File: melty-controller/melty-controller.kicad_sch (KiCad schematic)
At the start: 39 parts, among them J1 Conn_01x02_Male, J2 soicbite, J3 esc_io, Q1 2N7002ET1G, U1 ESP32-PICO-D4, U2 MT2492, U3 MMA1200KEG, U4 HT7250

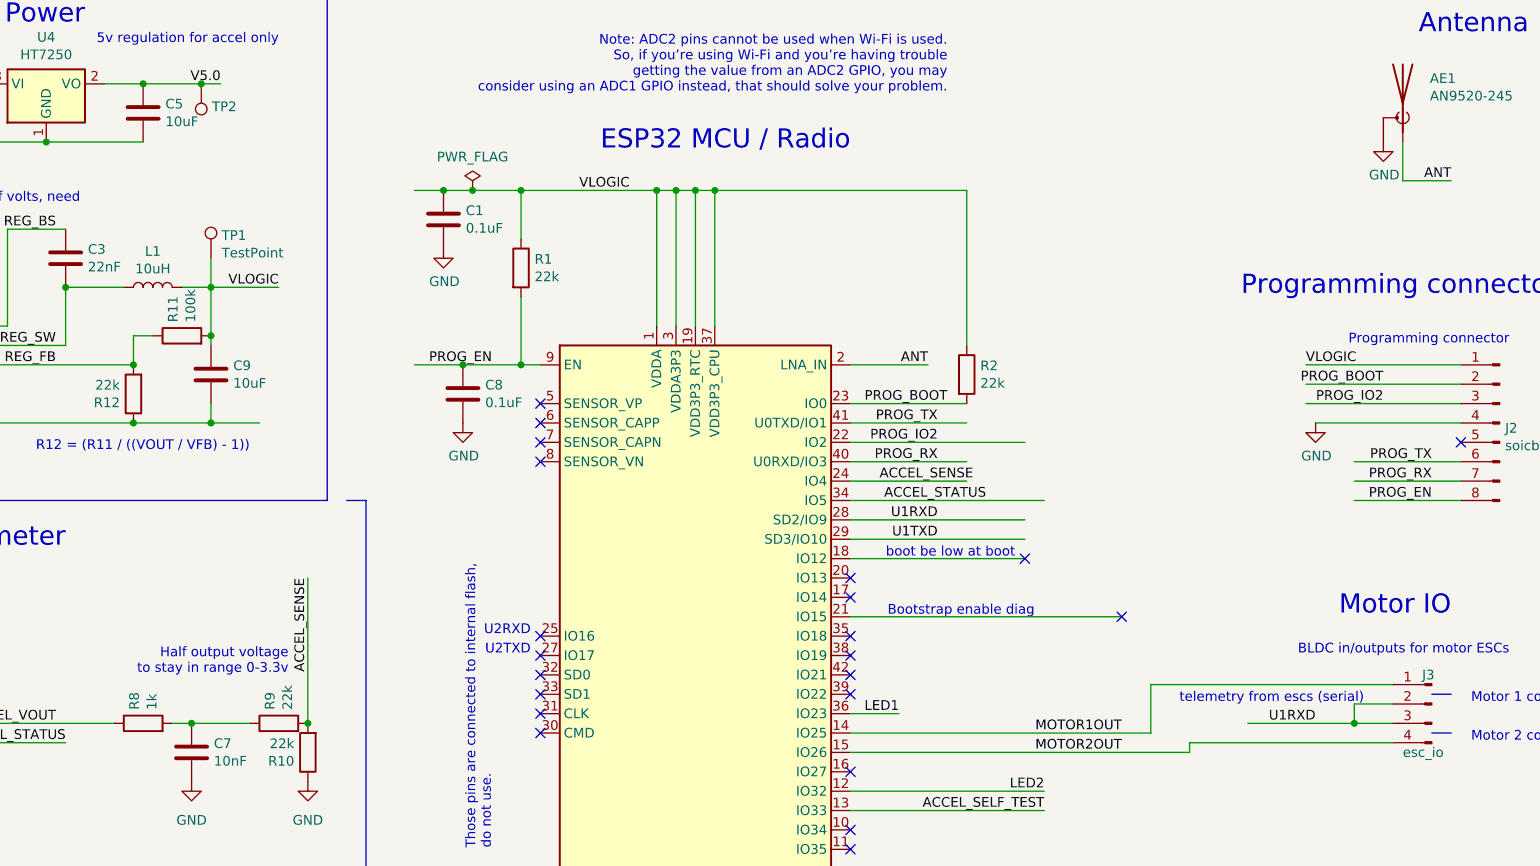
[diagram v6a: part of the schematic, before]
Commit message: Add more testpoints and minor fixes
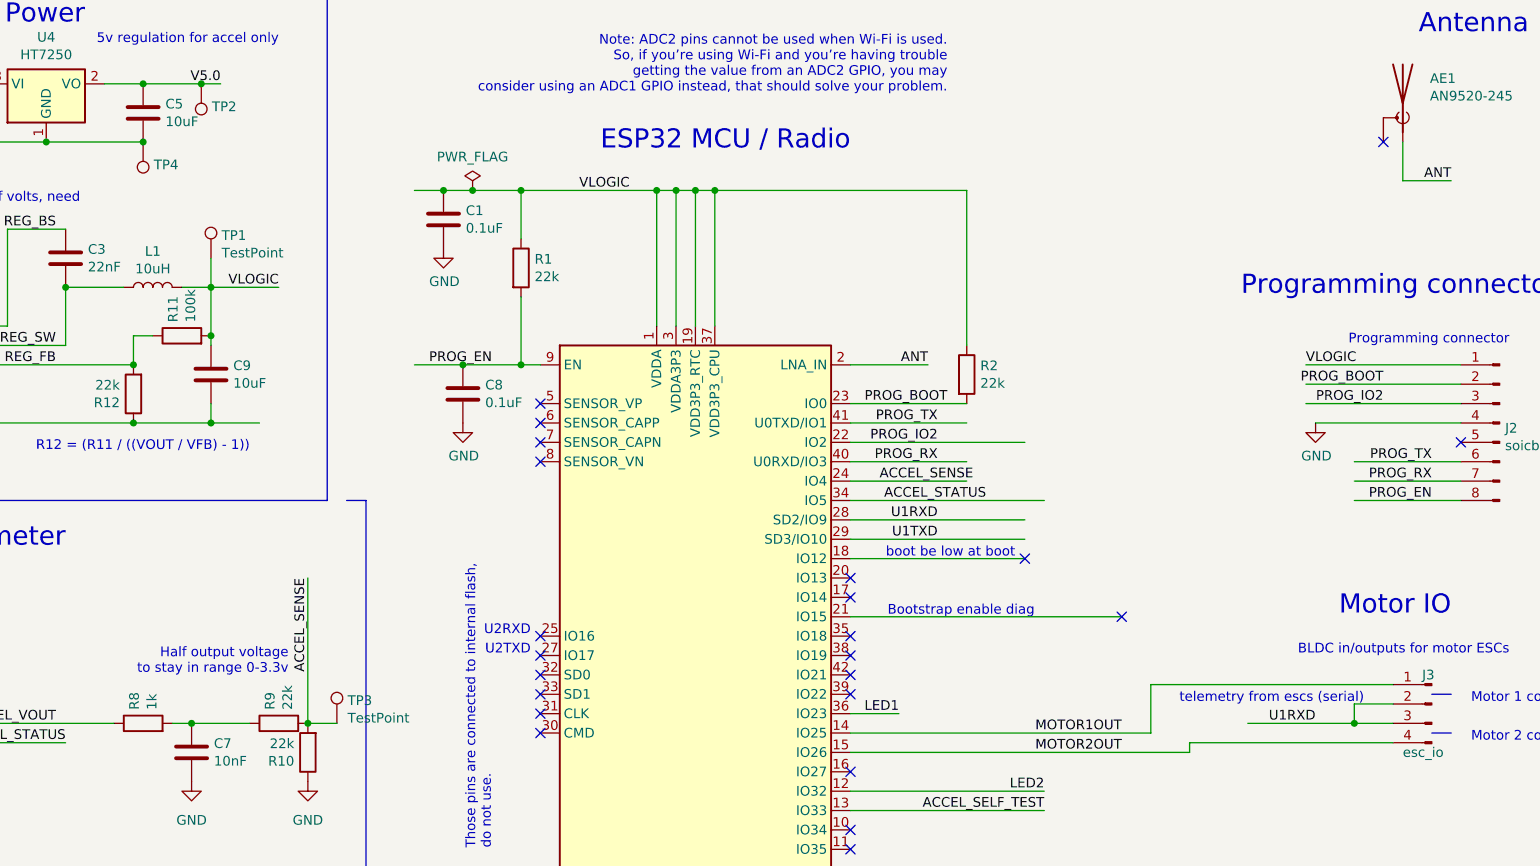
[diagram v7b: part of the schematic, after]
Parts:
- added TP3, TP4: TestPoint, TestPoint:TestPoint_Pad_1.5x1.5mm, symbol Connector:TestPoint
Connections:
- net ACCEL_SENSE: now also TP3.1
- net GND: now also TP4.1; no longer AE1.2 (Shield)
- no-connect marks 22 -> 23
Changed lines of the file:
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@@
   (junction (at 77.47 71.12) (diameter 0) (color 0 0 0 0))
   (junction (at 78.74 26.67) (diameter 0) (color 0 0 0 0))
+  (junction (at 78.74 34.29) (diameter 0) (color 0 0 0 0))
   (junction (at 83.82 173.99) (diameter 0) (color 0 0 0 0))
   (junction (at 85.09 110.49) (diameter 0) (color 0 0 0 0))
@@
   (junction (at 153.67 40.64) (diameter 0) (color 0 0 0 0))
   (junction (at 237.49 110.49) (diameter 0) (color 0 0 0 0))
-  (no_connect (at 171.45 99.06))
-  (no_connect (at 171.45 116.84))
-  (no_connect (at 171.45 101.6))
+  (no_connect (at 130.81 71.12))
+  (no_connect (at 130.81 68.58))
+  (no_connect (at 171.45 104.14))
   (no_connect (at 251.46 73.66))
-  (no_connect (at 130.81 68.58))
+  (no_connect (at 171.45 127))
+  (no_connect (at 207.01 96.52))
+  (no_connect (at 194.31 88.9))
   (no_connect (at 171.45 124.46))
-  (no_connect (at 171.45 91.44))
+  (no_connect (at 171.45 106.68))
+  (no_connect (at 130.81 101.6))
+  (no_connect (at 130.81 111.76))
+  (no_connect (at 171.45 93.98))
   (no_connect (at 130.81 109.22))
-  (no_connect (at 207.01 96.52))
   (no_connect (at 130.81 73.66))
   (no_connect (at 130.81 106.68))
-  (no_connect (at 171.45 127))
+  (no_connect (at 171.45 91.44))
+  (no_connect (at 130.81 104.14))
+  (no_connect (at 171.45 99.06))
   (no_connect (at 130.81 76.2))
-  (no_connect (at 171.45 104.14))
-  (no_connect (at 171.45 93.98))
-  (no_connect (at 130.81 71.12))
-  (no_connect (at 130.81 101.6))
-  (no_connect (at 171.45 106.68))
-  (no_connect (at 130.81 104.14))
-  (no_connect (at 130.81 111.76))
-  (no_connect (at 194.31 88.9))
+  (no_connect (at 171.45 116.84))
   (no_connect (at 130.81 99.06))
+  (no_connect (at 171.45 101.6))
+  (no_connect (at 241.3 34.29))
   (wire (pts (xy 15.24 118.11) (xy 33.02 118.11))
     (stroke (width 0) (type solid) (color 0 0 0 0))
@@
   )
   (wire (pts (xy 100.33 91.44) (xy 100.33 110.49))
+    (stroke (width 0) (type solid) (color 0 0 0 0))
+  )
+  (wire (pts (xy 100.33 110.49) (xy 104.14 110.49))
     (stroke (width 0) (type solid) (color 0 0 0 0))
   )
@@
     )
   )
+  (symbol (lib_id "Connector:TestPoint") (at 78.74 34.29 0) (mirror x) (unit 1)
+    (in_bom yes) (on_board yes)
+    (property "Reference" "TP4" (id 0) (at 80.1371 37.2809 0)
+      (effects (font (size 1.27 1.27)) (justify left))
+    )
+    (property "Value" "TestPoint" (id 1) (at 80.1371 34.9822 0)
+      (effects (font (size 1.27 1.27)) (justify left) hide)
+    )
+    (property "Footprint" "TestPoint:TestPoint_Pad_1.5x1.5mm" (id 2) (at 83.82 34.29 0)
+      (effects (font (size 1.27 1.27)) hide)
+    )
+    (property "Datasheet" "~" (id 3) (at 83.82 34.29 0)
+      (effects (font (size 1.27 1.27)) hide)
+    )
+  )
   (symbol (lib_id "Connector:TestPoint") (at 86.36 26.67 0) (mirror x) (unit 1)
     (in_bom yes) (on_board yes)
@@
     )
     (property "Datasheet" "~" (id 3) (at 92.71 49.53 0)
+      (effects (font (size 1.27 1.27)) hide)
+    )
+  )
+  (symbol (lib_id "Connector:TestPoint") (at 104.14 110.49 0) (unit 1)
+    (in_bom yes) (on_board yes)
+    (property "Reference" "TP3" (id 0) (at 105.5371 107.4991 0)
+      (effects (font (size 1.27 1.27)) (justify left))
+    )
+    (property "Value" "TestPoint" (id 1) (at 105.5371 109.7978 0)
+      (effects (font (size 1.27 1.27)) (justify left))
+    )
+    (property "Footprint" "TestPoint:TestPoint_Pad_1.5x1.5mm" (id 2) (at 109.22 110.49 0)
+      (effects (font (size 1.27 1.27)) hide)
+    )
+    (property "Datasheet" "~" (id 3) (at 109.22 110.49 0)
       (effects (font (size 1.27 1.27)) hide)
     )
@@
     )
     (property "Datasheet" "" (id 3) (at 232.41 71.12 0)
-      (effects (font (size 1.27 1.27)) hide)
-    )
-  )
-  (symbol (lib_id "power:GND") (at 241.3 34.29 0) (unit 1)
-    (in_bom yes) (on_board yes)
-    (property "Reference" "#PWR04" (id 0) (at 241.3 40.64 0)
-      (effects (font (size 1.27 1.27)) hide)
-    )
-    (property "Value" "GND" (id 1) (at 241.4143 38.6144 0))
-    (property "Footprint" "" (id 2) (at 241.3 34.29 0)
-      (effects (font (size 1.27 1.27)) hide)
-    )
-    (property "Datasheet" "" (id 3) (at 241.3 34.29 0)
       (effects (font (size 1.27 1.27)) hide)
     )
@@
       (reference "#PWR03") (unit 1)
     )
-    (path "/443ac6f1-680f-4598-9ffb-e96eef2d7f1a"
-      (reference "#PWR04") (unit 1)
-    )
     (path "/f0666eca-ac18-44f5-a55d-51e5ed066097"
       (reference "#PWR05") (unit 1)
@@
       (reference "TP2") (unit 1)
     )
+    (path "/6a4587a3-cf5e-4524-a8c1-3f68fefec719"
+      (reference "TP3") (unit 1)
+    )
+    (path "/351c7b9e-3c3a-4f95-85df-106866db9b8b"
+      (reference "TP4") (unit 1)
+    )
     (path "/b91b9274-ad09-4c59-9311-b440a305e6c7"

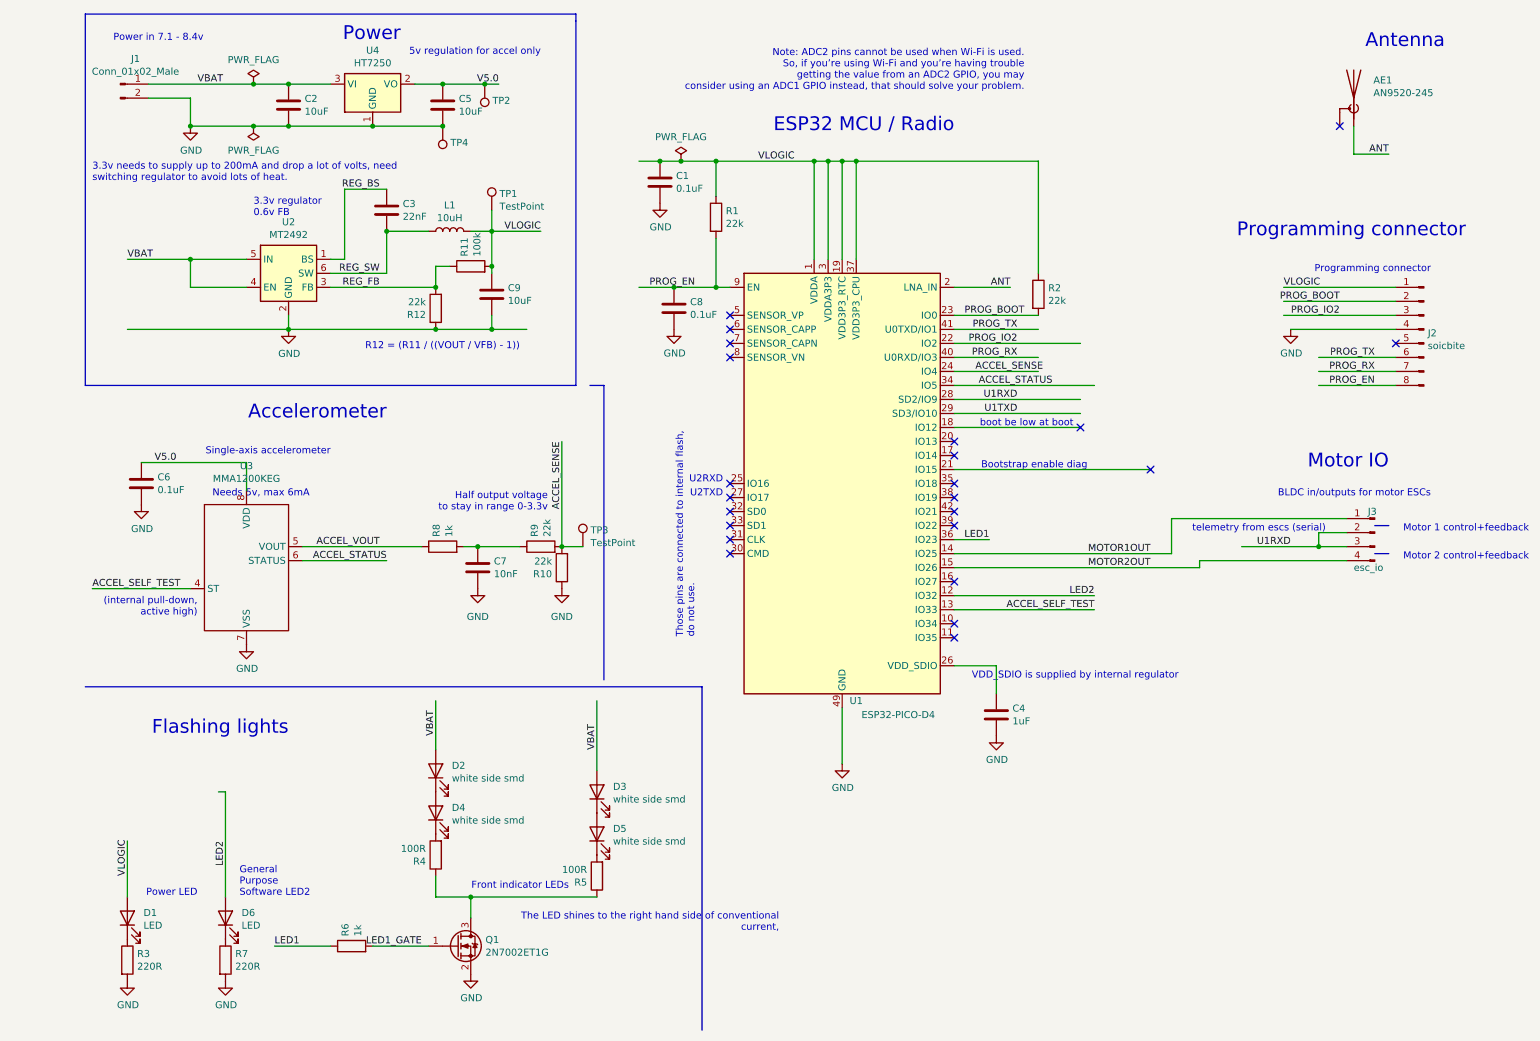
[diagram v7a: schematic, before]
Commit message: correct some doc errors on schematic
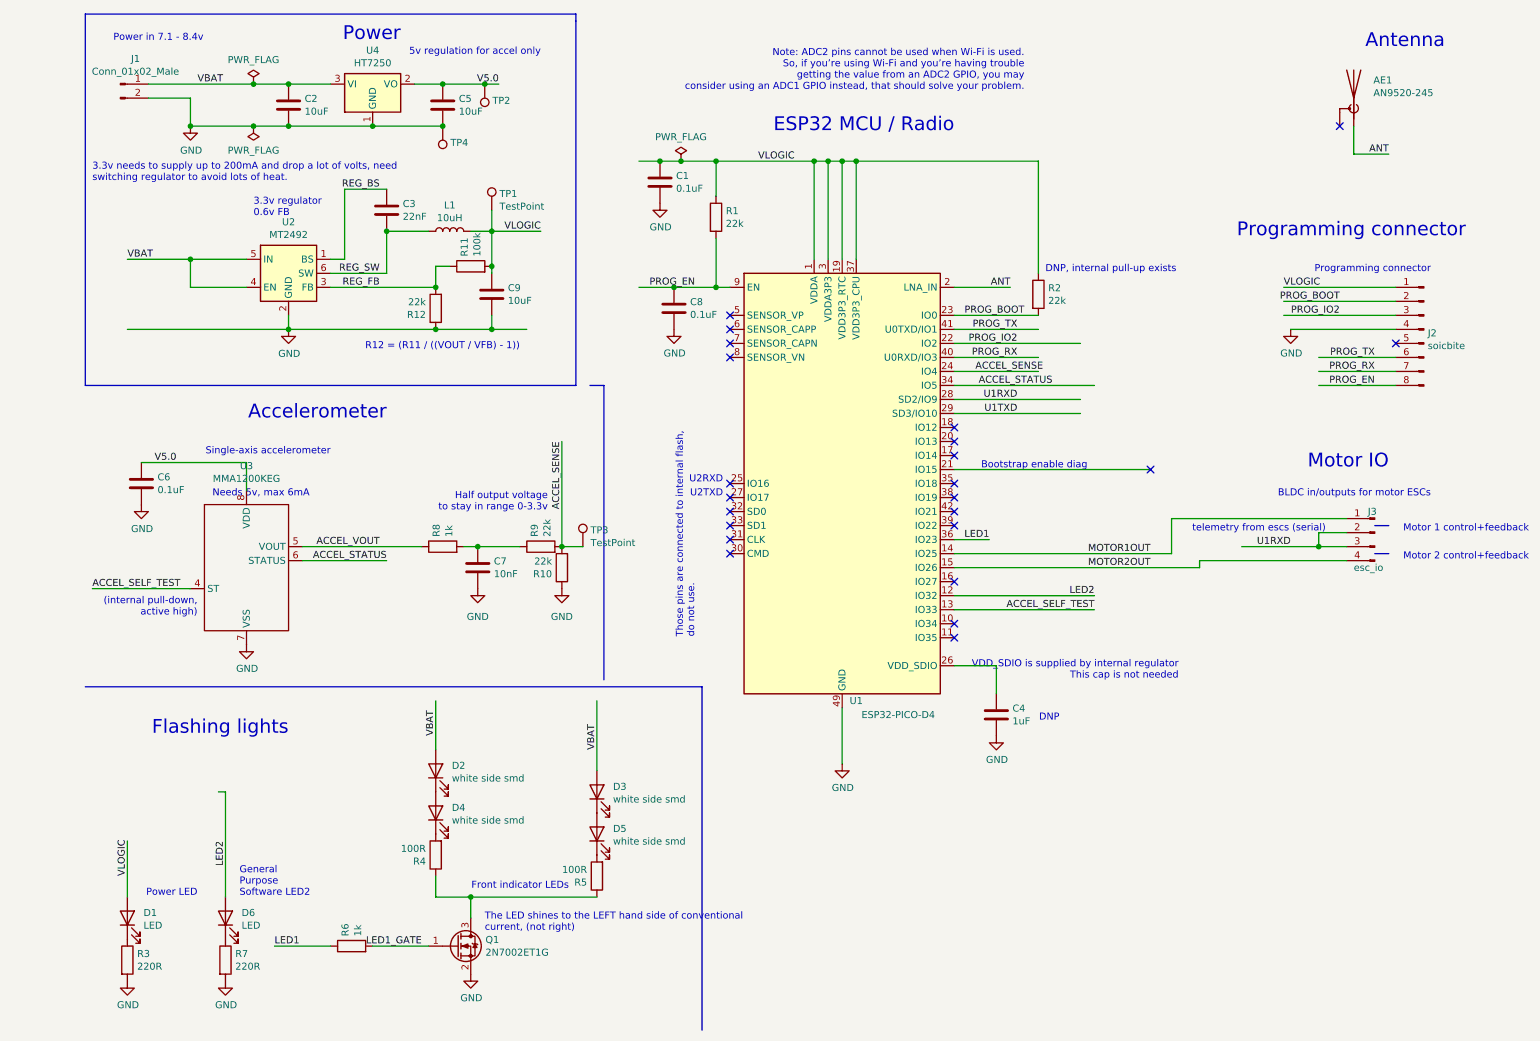
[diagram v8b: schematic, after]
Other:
- note added: "DNP"
- note added: "DNP, internal pull-up exists"
- note added: "The LED shines to the LEFT hand side of conventional current, (not right)"
- note added: "VDD_SDIO is supplied by internal regulator This cap is not needed"
- note removed: "The LED shines to the right hand side of conventional current,"
- note removed: "VDD_SDIO is supplied by internal regulator"
- note removed: "boot be low at boot"
